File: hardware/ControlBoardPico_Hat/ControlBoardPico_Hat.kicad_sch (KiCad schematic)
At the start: 31 parts, among them J1 I2C, J10 Button 4, J11 Button 5, J12 LinAct, J13 SpCtr, J14 RC, J15 VOL, J16 LED 1, J17 RevSw, J18 LED 2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

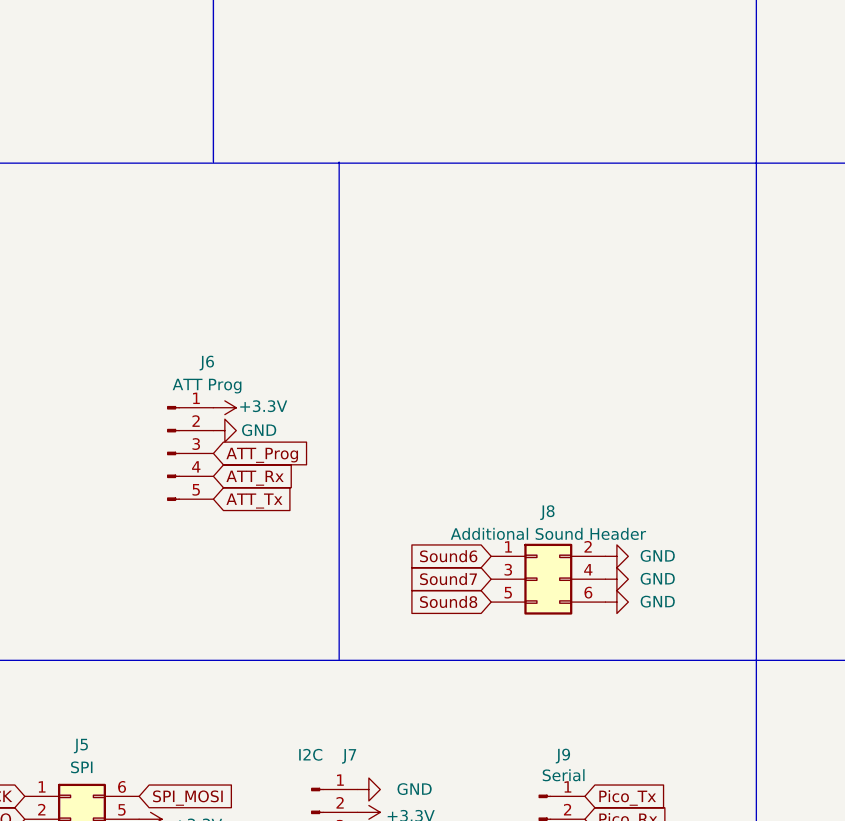
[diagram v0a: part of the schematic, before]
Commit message: Whack-a-mole Pico HAT PCB clean up
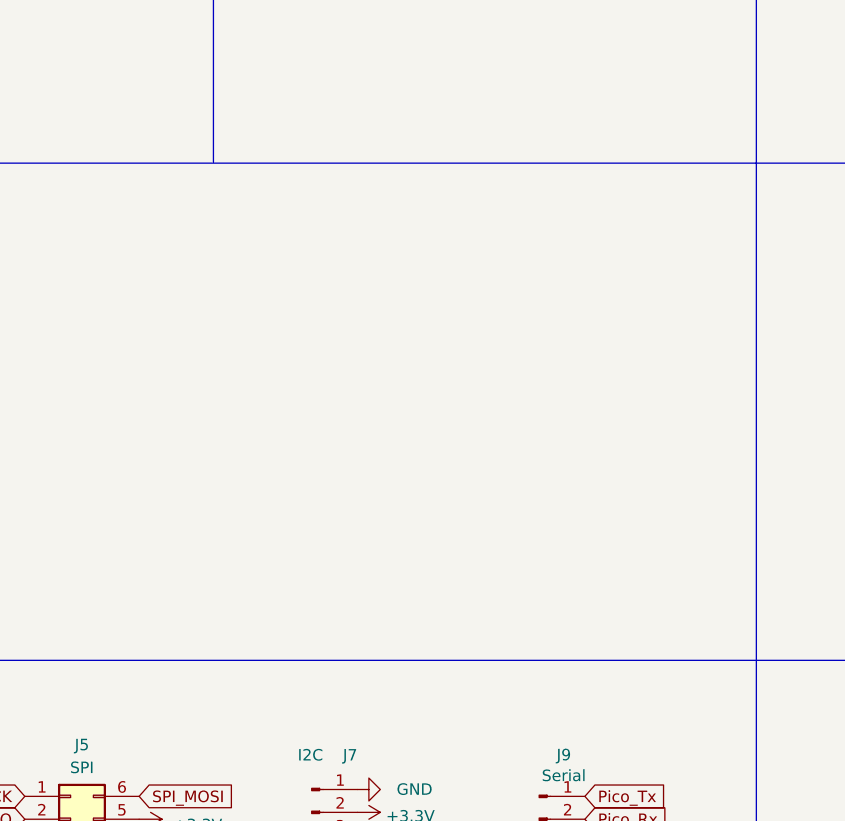
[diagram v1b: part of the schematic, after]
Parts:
- removed J6: ATT Prog, Connector_PinHeader_2.54mm:PinHeader_1x05_P2.54mm_Vertical, symbol Connector:Conn_01x05_Pin
- removed J8: Additional Sound Header, Connector_PinSocket_2.54mm:PinSocket_2x03_P2.54mm_Vertical, symbol Connector_Generic:Conn_02x03_Odd_Even
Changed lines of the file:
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@@
-    (stroke (width 0) (type default))
-  )
-  (polyline (pts (xy 123.825 139.7) (xy 123.825 84.455))
     (stroke (width 0) (type default))
   )
@@
     )
   )
-  (global_label "ATT_Rx" (shape input) (at 109.855 119.38 0) (fields_autoplaced)
-    (effects (font (size 1.27 1.27)) (justify left))
-    (property "Intersheetrefs" "${INTERSHEET_REFS}" (at 118.3961 119.38 0)
-      (effects (font (size 1.27 1.27)) (justify left) hide)
-    )
-  )
   (global_label "SPI_SCK" (shape input) (at 73.66 35.56 180) (fields_autoplaced)
     (effects (font (size 1.27 1.27)) (justify right))
@@
     )
   )
-  (global_label "Sound6" (shape input) (at 140.716 128.27 180) (fields_autoplaced)
-    (effects (font (size 1.27 1.27)) (justify right))
-    (property "Intersheetrefs" "${INTERSHEET_REFS}" (at 131.37 128.27 0)
-      (effects (font (size 1.27 1.27)) (justify right) hide)
-    )
-  )
   (global_label "ReverseSwitch" (shape input) (at 73.66 38.1 180) (fields_autoplaced)
     (effects (font (size 1.27 1.27)) (justify right))
@@
     )
   )
-  (global_label "ATT_Tx" (shape input) (at 109.855 121.92 0) (fields_autoplaced)
-    (effects (font (size 1.27 1.27)) (justify left))
-    (property "Intersheetrefs" "${INTERSHEET_REFS}" (at 118.0937 121.92 0)
-      (effects (font (size 1.27 1.27)) (justify left) hide)
-    )
-  )
   (global_label "LED_3_TRIGGER" (shape input) (at 77.47 33.02 0) (fields_autoplaced)
     (effects (font (size 1.27 1.27)) (justify left))
@@
     )
   )
-  (global_label "Sound8" (shape input) (at 140.716 133.35 180) (fields_autoplaced)
-    (effects (font (size 1.27 1.27)) (justify right))
-    (property "Intersheetrefs" "${INTERSHEET_REFS}" (at 131.3766 133.4294 0)
-      (effects (font (size 1.27 1.27)) (justify right) hide)
-    )
-  )
   (global_label "I2C_SCL" (shape input) (at 125.857 161.798 0) (fields_autoplaced)
     (effects (font (size 1.27 1.27)) (justify left))
@@
     )
   )
-  (global_label "Sound7" (shape input) (at 140.716 130.81 180) (fields_autoplaced)
-    (effects (font (size 1.27 1.27)) (justify right))
-    (property "Intersheetrefs" "${INTERSHEET_REFS}" (at -81.915 3.175 0)
-      (effects (font (size 1.27 1.27)) hide)
-    )
-  )
   (global_label "BUTTON_3" (shape input) (at 77.47 48.26 0) (fields_autoplaced)
     (effects (font (size 1.27 1.27)) (justify left))
@@
     (effects (font (size 1.27 1.27)) (justify left))
     (property "Intersheetrefs" "${INTERSHEET_REFS}" (at 110.4624 160.02 0)
-      (effects (font (size 1.27 1.27)) (justify left) hide)
-    )
-  )
-  (global_label "ATT_Prog" (shape input) (at 109.855 116.84 0) (fields_autoplaced)
-    (effects (font (size 1.27 1.27)) (justify left))
-    (property "Intersheetrefs" "${INTERSHEET_REFS}" (at 120.5249 116.7606 0)
       (effects (font (size 1.27 1.27)) (justify left) hide)
     )
@@
     )
   )
-  (symbol (lib_id "power:GND") (at 153.416 128.27 90) (unit 1)
-    (in_bom yes) (on_board yes) (dnp no)
-    (property "Reference" "#PWR018" (at 159.766 128.27 0)
-      (effects (font (size 1.27 1.27)) hide)
-    )
-    (property "Value" "GND" (at 157.226 128.27 90)
-      (effects (font (size 1.27 1.27)) (justify right))
-    )
-    (property "Footprint" "" (at 153.416 128.27 0)
-      (effects (font (size 1.27 1.27)) hide)
-    )
-    (property "Datasheet" "" (at 153.416 128.27 0)
-      (effects (font (size 1.27 1.27)) hide)
-    )
-    (pin "1")
-    (instances
-      (project "ControlBoardPico_Hat"
-        (path "/ee7e864e-15ea-4ba5-a64c-c53b37d2e4fb"
-          (reference "#PWR018") (unit 1)
-        )
-      )
-    )
-  )
-  (symbol (lib_id "power:GND") (at 153.416 130.81 90) (unit 1)
-    (in_bom yes) (on_board yes) (dnp no)
-    (property "Reference" "#PWR019" (at 159.766 130.81 0)
-      (effects (font (size 1.27 1.27)) hide)
-    )
-    (property "Value" "GND" (at 157.226 130.81 90)
-      (effects (font (size 1.27 1.27)) (justify right))
-    )
-    (property "Footprint" "" (at 153.416 130.81 0)
-      (effects (font (size 1.27 1.27)) hide)
-    )
-    (property "Datasheet" "" (at 153.416 130.81 0)
-      (effects (font (size 1.27 1.27)) hide)
-    )
-    (pin "1")
-    (instances
-      (project "ControlBoardPico_Hat"
-        (path "/ee7e864e-15ea-4ba5-a64c-c53b37d2e4fb"
-          (reference "#PWR019") (unit 1)
-        )
-      )
-    )
-  )
-  (symbol (lib_id "power:GND") (at 153.416 133.35 90) (unit 1)
-    (in_bom yes) (on_board yes) (dnp no)
-    (property "Reference" "#PWR020" (at 159.766 133.35 0)
-      (effects (font (size 1.27 1.27)) hide)
-    )
-    (property "Value" "GND" (at 157.226 133.35 90)
-      (effects (font (size 1.27 1.27)) (justify right))
-    )
-    (property "Footprint" "" (at 153.416 133.35 0)
-      (effects (font (size 1.27 1.27)) hide)
-    )
-    (property "Datasheet" "" (at 153.416 133.35 0)
-      (effects (font (size 1.27 1.27)) hide)
-    )
-    (pin "1")
-    (instances
-      (project "ControlBoardPico_Hat"
-        (path "/ee7e864e-15ea-4ba5-a64c-c53b37d2e4fb"
-          (reference "#PWR020") (unit 1)
-        )
-      )
-    )
-  )
   (symbol (lib_id "power:GND") (at 250.825 99.695 90) (unit 1)
     (in_bom yes) (on_board yes) (dnp no)
@@
     )
   )
-  (symbol (lib_id "power:+3.3V") (at 109.855 111.76 270) (unit 1)
-    (in_bom yes) (on_board yes) (dnp no)
-    (property "Reference" "#PWR010" (at 106.045 111.76 0)
-      (effects (font (size 1.27 1.27)) hide)
-    )
-    (property "Value" "+3.3V" (at 112.649 111.633 90)
-      (effects (font (size 1.27 1.27)) (justify left))
-    )
-    (property "Footprint" "" (at 109.855 111.76 0)
-      (effects (font (size 1.27 1.27)) hide)
-    )
-    (property "Datasheet" "" (at 109.855 111.76 0)
-      (effects (font (size 1.27 1.27)) hide)
-    )
-    (pin "1")
-    (instances
-      (project "ControlBoardPico_Hat"
-        (path "/ee7e864e-15ea-4ba5-a64c-c53b37d2e4fb"
-          (reference "#PWR010") (unit 1)
-        )
-      )
-    )
-  )
   (symbol (lib_id "Connector:Conn_01x02_Pin") (at 212.09 131.445 0) (unit 1)
     (in_bom no) (on_board yes) (dnp no)
@@
     )
   )
-  (symbol (lib_id "Connector:Conn_01x05_Pin") (at 104.775 116.84 0) (unit 1)
-    (in_bom no) (on_board yes) (dnp no)
-    (property "Reference" "J6" (at 109.22 106.68 0)
-      (effects (font (size 1.27 1.27)))
-    )
-    (property "Value" "ATT Prog" (at 109.22 109.22 0)
-      (effects (font (size 1.27 1.27)))
-    )
-    (property "Footprint" "Connector_PinHeader_2.54mm:PinHeader_1x05_P2.54mm_Vertical" (at 104.775 116.84 0)
-      (effects (font (size 1.27 1.27)) hide)
-    )
-    (property "Datasheet" "~" (at 104.775 116.84 0)
-      (effects (font (size 1.27 1.27)) hide)
-    )
-    (pin "1")
-    (pin "2")
-    (pin "3")
-    (pin "4")
-    (pin "5")
-    (instances
-      (project "ControlBoardPico_Hat"
-        (path "/ee7e864e-15ea-4ba5-a64c-c53b37d2e4fb"
-          (reference "J6") (unit 1)
-        )
-      )
-    )
-  )
-  (symbol (lib_id "Connector_Generic:Conn_02x03_Odd_Even") (at 145.796 130.81 0) (unit 1)
-    (in_bom no) (on_board yes) (dnp no) (fields_autoplaced)
-    (property "Reference" "J8" (at 147.066 123.3002 0)
-      (effects (font (size 1.27 1.27)))
-    )
-    (property "Value" "Additional Sound Header" (at 147.066 125.8371 0)
-      (effects (font (size 1.27 1.27)))
-    )
-    (property "Footprint" "Connector_PinSocket_2.54mm:PinSocket_2x03_P2.54mm_Vertical" (at 145.796 130.81 0)
-      (effects (font (size 1.27 1.27)) hide)
-    )
-    (property "Datasheet" "~" (at 145.796 130.81 0)
-      (effects (font (size 1.27 1.27)) hide)
-    )
-    (pin "1")
-    (pin "2")
-    (pin "3")
-    (pin "4")
-    (pin "5")
-    (pin "6")
-    (instances
-      (project "ControlBoardPico_Hat"
-        (path "/ee7e864e-15ea-4ba5-a64c-c53b37d2e4fb"
-          (reference "J8") (unit 1)
-        )
-      )
-    )
-  )
   (symbol (lib_id "power:GND") (at 234.95 57.15 0) (unit 1)
     (in_bom yes) (on_board yes) (dnp no)
@@
         )
       )
-    )
-  )
-  (symbol (lib_id "power:GND") (at 109.855 114.3 90) (unit 1)
-    (in_bom yes) (on_board yes) (dnp no)
-    (property "Reference" "#PWR011" (at 116.205 114.3 0)
-      (effects (font (size 1.27 1.27)) hide)
-    )
-    (property "Value" "GND" (at 114.935 114.3 90)
-      (effects (font (size 1.27 1.27)))
-    )
-    (property "Footprint" "" (at 109.855 114.3 0)
-      (effects (font (size 1.27 1.27)) hide)
-    )
-    (property "Datasheet" "" (at 109.855 114.3 0)
-      (effects (font (size 1.27 1.27)) hide)
-    )
-    (pin "1")
-    (instances
-      (project "ControlBoardPico_Hat"
-        (path "/ee7e864e-15ea-4ba5-a64c-c53b37d2e4fb"
-          (reference "#PWR011") (unit 1)
-        )
-      )
